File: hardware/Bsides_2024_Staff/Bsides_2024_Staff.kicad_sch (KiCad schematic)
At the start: 32 parts, among them J1 UART, J2 Battery, J3 OLED, J4 I2C, P1 USB_C_Plug_USB2.0, Q1 DMG3415U-7, SW1 ON, SW2 RESET, SW3 GPIO, SW4 RESET, SW5 RESET, SW6 RESET, SW7 RESET, U1 ESP32-C6-WROOM-1U-N4, U2 AP2112K-3.3

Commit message: feat(Hw):Init_Floorplan
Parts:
- SW1: footprint Footprint:JS102011SAQN -> bsides:MSK12C02
- SW3: value GPIO -> BOOT
- SW5, SW7: value RESET -> ~
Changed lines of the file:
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@@
 			)
 		)
-		(property "Footprint" "Footprint:JS102011SAQN"
+		(property "Footprint" "bsides:MSK12C02"
 			(at 45.339 176.276 0)
 			(effects
@@
 			)
 		)
-		(property "Value" "RESET"
+		(property "Value" "~"
 			(at 257.429 62.8904 0)
 			(effects
@@
 					(size 1.27 1.27)
 				)
+				(hide yes)
 			)
 		)
@@
 					(size 1.27 1.27)
 				)
+				(hide yes)
 			)
 		)
@@
 			)
 		)
-		(property "Value" "GPIO"
+		(property "Value" "BOOT"
 			(at 176.911 46.99 0)
 			(effects
@@
 		(dnp no)
 		(property "Reference" "SW7"
-			(at 259.461 43.815 0)
+			(at 259.334 46.228 0)
 			(effects
 				(font
@@
 			)
 		)
-		(property "Value" "RESET"
+		(property "Value" "~"
 			(at 259.461 46.1264 0)
 			(effects
@@
 					(size 1.27 1.27)
 				)
+				(hide yes)
 			)
 		)

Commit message: feat(Hw):Add_Preview
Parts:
- removed D2: RED, LED_SMD:LED_0805_2012Metric, symbol Device:LED_Small
- removed J1: UART, Connector_PinHeader_2.54mm:PinHeader_1x05_P2.54mm_Vertical, symbol Connector:Screw_Terminal_01x05
- removed J4: I2C, Connector_PinHeader_2.54mm:PinHeader_1x04_P2.54mm_Vertical, symbol Connector:Screw_Terminal_01x04
- removed R6: 330R, Resistor_SMD:R_0805_2012Metric_Pad1.20x1.40mm_HandSolder, symbol Device:R_Small
- added C10, C11, C12, C9: 0.1uF, Capacitor_SMD:C_0603_1608Metric, symbol Device:C
- added D2, D3, D4, D5: WS2812B, LED_SMD:LED_WS2812B-Mini_PLCC4_3.5x3.5mm, symbol LED:WS2812B
- added J1: Battery, bsides:BH-AAA-A1aj001, symbol Connector:Screw_Terminal_01x02
- added J4: Conn_02x03_Odd_Even, Connector_PinSocket_2.54mm:PinSocket_2x03_P2.54mm_Vertical, symbol Connector_Generic:Conn_02x03_Odd_Even
- added R7: 470, Resistor_SMD:R_0603_1608Metric, symbol Device:R
- C3, C4: value .1uF -> 0.1uF
- C5, C6, C7, C8: footprint (none) -> Capacitor_SMD:C_0603_1608Metric
- J2: footprint Footprint:BAT-TH_BH-AAA-A1AJ024 -> bsides:BH-AAA-A1aj001
- J3: footprint Connector_PinHeader_2.54mm:PinHeader_1x04_P2.54mm_Vertical -> bsides:Display OLED 128 x32
- P1: footprint Footprint:C393939 -> bsides:C393939
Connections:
- net +3V3: now also C10.2, C11.2, C12.2, C9.2, D2.1 (VDD), D3.1 (VDD), D4.1 (VDD), D5.1 (VDD)
- net GND: now also C10.1, C11.1, C12.1, C9.1, D2.3 (VSS), D3.3 (VSS), D4.3 (VSS), D5.3 (VSS), J1.1 (Pin_1); no longer J2.1 (Pin_1)
- net LED1 renamed PIN
- net PIN: now also R7.1
- new net: D2.4 (DIN), D5.2 (DOUT)
- new net: D4.2 (DOUT), D5.4 (DIN)
- new net: D3.2 (DOUT), D4.4 (DIN)
- new net: J1.2 (Pin_2), J2.1 (Pin_1)
- new net: D3.4 (DIN), R7.2
- no-connect marks 12 -> 13

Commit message: feat:(Hw)Update_PCB_Speaker_Sponsor_Staff
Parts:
- added C13: 1uF, Capacitor_SMD:C_0603_1608Metric, symbol Device:C_Small
- added C14, C15: 10uF, Capacitor_SMD:C_0603_1608Metric, symbol Device:C_Small
- J1, J2: footprint bsides:BH-AAA-A1aj001 -> bsides:BH-AA-A1AJ020; LCSC# C5290193 -> (none)
- J4: value Conn_02x03_Odd_Even -> Add_On
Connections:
- net GND: now also J4.2 (Pin_2), C13.2, C14.2, C15.2
- net SCL: now also J4.4 (Pin_4)
- net SDA: now also J4.3 (Pin_3)
- net VBUS: now also C1.1, U2.1 (VIN), U2.3 (EN); no longer D1.2 (A), Q1.1 (G), R2.1
- net VOUT: now reaches J4.1 (Pin_1)
- net VOUT: now also C10.2, C11.2, C12.2, C9.2, D2.1 (VDD), D3.1 (VDD), D4.1 (VDD), D5.1 (VDD), J3.1 (Pin_1), R1.2, R5.2, SW1.2 (B), U1.2 (3V3), C13.1, C14.1, C15.1
- removed net +3V3: C10.2, C11.2, C12.2, C2.1, C9.2, D2.1 (VDD), D3.1 (VDD), D4.1 (VDD), D5.1 (VDD), J3.1 (Pin_1), R1.2, R5.2, U1.2 (3V3), U2.5 (VOUT)
- new net: C2.1, D1.2 (A), Q1.1 (G), R2.1, U2.5 (VOUT)
- no-connect marks 13 -> 15
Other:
- moved on the sheet: D1, J1, J2, Q1, R1, R2, SW1, U1

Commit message: feat(Hw): Update schematics
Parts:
- J3: manf# I2C SH1106 Display Oled Azul 128×64 1.3 ” -> Display OLED 128×32 0.91 I2C SSD1306 Blanco / Azul
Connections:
- net GND: now also J3.4 (Pin_4); no longer J3.2 (Pin_2)
- net SCL: now also J3.2 (Pin_2); no longer J3.3 (Pin_3)
- net SDA: now also J3.1 (Pin_1); no longer J3.4 (Pin_4)
- net VOUT: now also J3.3 (Pin_3); no longer J3.1 (Pin_1)
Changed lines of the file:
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@@
 	(wire
 		(pts
+			(xy 82.55 124.46) (xy 80.01 124.46)
+		)
+		(stroke
+			(width 0)
+			(type default)
+		)
+	)
+	(wire
+		(pts
 			(xy 69.088 51.816) (xy 81.026 51.816)
 		)
@@
 	(wire
 		(pts
+			(xy 82.55 119.38) (xy 80.01 119.38)
+		)
+		(stroke
+			(width 0)
+			(type default)
+		)
+	)
+	(wire
+		(pts
 			(xy 121.412 41.91) (xy 124.46 41.91)
 		)
@@
 	(wire
 		(pts
+			(xy 82.55 116.84) (xy 80.01 116.84)
+		)
+		(stroke
+			(width 0)
+			(type default)
+		)
+	)
+	(wire
+		(pts
 			(xy 81.026 40.132) (xy 81.026 43.18)
 		)
@@
 	(wire
 		(pts
-			(xy 95.504 135.636) (xy 101.854 135.636)
-		)
-		(stroke
-			(width 0)
-			(type default)
-		)
-	)
-	(wire
-		(pts
 			(xy 54.102 178.308) (xy 54.102 176.276)
 		)
@@
 	(wire
 		(pts
-			(xy 95.504 130.556) (xy 101.854 130.556)
-		)
-		(stroke
-			(width 0)
-			(type default)
-		)
-	)
-	(wire
-		(pts
 			(xy 166.497 52.324) (xy 162.941 52.324)
 		)
@@
 	(wire
 		(pts
-			(xy 95.504 133.096) (xy 101.854 133.096)
-		)
-		(stroke
-			(width 0)
-			(type default)
-		)
-	)
-	(wire
-		(pts
 			(xy 213.614 121.539) (xy 217.424 121.539)
 		)
@@
 	(wire
 		(pts
-			(xy 95.504 128.016) (xy 101.854 128.016)
-		)
-		(stroke
-			(width 0)
-			(type default)
-		)
-	)
-	(wire
-		(pts
 			(xy 36.576 30.988) (xy 36.576 33.528)
 		)
@@
 	(wire
 		(pts
+			(xy 82.55 121.92) (xy 80.01 121.92)
+		)
+		(stroke
+			(width 0)
+			(type default)
+		)
+	)
+	(wire
+		(pts
 			(xy 262.255 87.376) (xy 265.049 87.376)
 		)
@@
 	)
 	(label "VOUT"
+		(at 80.01 121.92 180)
+		(fields_autoplaced yes)
+		(effects
+			(font
+				(size 1.27 1.27)
+			)
+			(justify right bottom)
+		)
+	)
+	(label "VOUT"
 		(at 238.252 119.888 0)
 		(fields_autoplaced yes)
@@
 		)
 	)
+	(label "SCL"
+		(at 80.01 119.38 180)
+		(fields_autoplaced yes)
+		(effects
+			(font
+				(size 1.27 1.27)
+			)
+			(justify right bottom)
+		)
+	)
 	(label "BOOT"
 		(at 35.052 70.612 0)
@@
 		)
 	)
+	(label "GND"
+		(at 80.01 124.46 180)
+		(fields_autoplaced yes)
+		(effects
+			(font
+				(size 1.27 1.27)
+			)
+			(justify right bottom)
+		)
+	)
 	(label "VOUT"
 		(at 113.792 182.626 0)
@@
 	)
 	(label "VOUT"
-		(at 95.504 128.016 0)
-		(fields_autoplaced yes)
-		(effects
-			(font
-				(size 1.27 1.27)
-			)
-			(justify left bottom)
-		)
-	)
-	(label "VOUT"
 		(at 18.034 80.264 0)
 		(fields_autoplaced yes)
@@
 		)
 	)
-	(label "GND"
-		(at 95.504 130.556 0)
-		(fields_autoplaced yes)
-		(effects
-			(font
-				(size 1.27 1.27)
-			)
-			(justify left bottom)
-		)
-	)
 	(label "EN"
 		(at 160.0454 36.576 180)
@@
 		)
 	)
-	(label "SCL"
-		(at 95.504 133.096 0)
-		(fields_autoplaced yes)
-		(effects
-			(font
-				(size 1.27 1.27)
-			)
-			(justify left bottom)
-		)
-	)
 	(label "VOUT"
 		(at 213.614 119.888 0)
@@
 		)
 	)
-	(label "RX"
-		(at 72.898 67.818 0)
+	(label "SDA"
+		(at 80.01 116.84 180)
 		(fields_autoplaced yes)
 		(effects
@@
 				(size 1.27 1.27)
 			)
-			(justify left bottom)
+			(justify right bottom)
 		)
 	)
-	(label "VOUT"
-		(at 27.432 54.61 0)
+	(label "RX"
+		(at 72.898 67.818 0)
 		(fields_autoplaced yes)
 		(effects
@@
 		)
 	)
-	(label "SDA"
-		(at 95.504 135.636 0)
+	(label "VOUT"
+		(at 27.432 54.61 0)
 		(fields_autoplaced yes)
 		(effects
@@
 	)
 	(symbol
-		(lib_id "Connector:Screw_Terminal_01x04")
-		(at 106.934 130.556 0)
-		(unit 1)
-		(exclude_from_sim no)
-		(in_bom yes)
-		(on_board yes)
-		(dnp no)
-		(fields_autoplaced yes)
-		(property "Reference" "J3"
-			(at 109.22 130.5559 0)
-			(effects
-				(font
-					(size 1.27 1.27)
-				)
-				(justify left)
-			)
-		)
-		(property "Value" "OLED"
-			(at 109.22 133.0959 0)
-			(effects
-				(font
-					(size 1.27 1.27)
-				)
-				(justify left)
-			)
-		)
-		(property "Footprint" "bsides:Display OLED 128 x32"
-			(at 106.934 130.556 0)
-			(effects
-				(font
-					(size 1.27 1.27)
-				)
-				(hide yes)
-			)
-		)
-		(property "Datasheet" "~"
-			(at 106.934 130.556 0)
-			(effects
-				(font
-					(size 1.27 1.27)
-				)
-				(hide yes)
-			)
-		)
-		(property "Description" ""
-			(at 106.934 130.556 0)
-			(effects
-				(font
-					(size 1.27 1.27)
-				)
-				(hide yes)
-			)
-		)
-		(property "manf#" "I2C SH1106 Display Oled Azul 128×64 1.3 ” "
-			(at 106.934 130.556 0)
-			(effects
-				(font
-					(size 1.27 1.27)
-				)
-				(hide yes)
-			)
-		)
-		(property "provedor" "UNIT Electronics"
-			(at 106.934 130.556 0)
-			(effects
-				(font
-					(size 1.27 1.27)
-				)
-				(hide yes)
-			)
-		)
-		(pin "1"
-		)
-		(pin "2"
-		)
-		(pin "3"
-		)
-		(pin "4"
-		)
-		(instances
-			(project "Bsides_2024_Staff"
-				(path "/93332268-4ddd-4d27-8a11-37637517d752"
-					(reference "J3")
-					(unit 1)
-				)
-			)
-		)
-	)
-	(symbol
 		(lib_id "HunterCat-NFC-rescue:USB_C_Plug_USB2.0-Connector")
 		(at 106.172 57.15 0)
@@
 					(unit 1)
 				)
+			)
+		)
+	)
+	(symbol
+		(lib_id "Connector:Screw_Terminal_01x04")
+		(at 87.63 119.38 0)
+		(unit 1)
+		(exclude_from_sim no)
+		(in_bom yes)
+		(on_board yes)
+		(dnp no)
+		(fields_autoplaced yes)
+		(property "Reference" "J3"
+			(at 89.916 119.3799 0)
+			(effects
+				(font
+					(size 1.27 1.27)
+				)
+				(justify left)
+			)
+		)
+		(property "Value" "OLED"
+			(at 89.916 121.9199 0)
+			(effects
+				(font
+					(size 1.27 1.27)
+				)
+				(justify left)
+			)
+		)
+		(property "Footprint" "bsides:Display OLED 128 x32"
+			(at 87.63 119.38 0)
+			(effects
+				(font
+					(size 1.27 1.27)
+				)
+				(hide yes)
+			)
+		)
+		(property "Datasheet" ""
+			(at 87.63 119.38 0)
+			(effects
+				(font
+					(size 1.27 1.27)
+				)
+				(hide yes)
+			)
+		)
+		(property "Description" ""
+			(at 87.63 119.38 0)
+			(effects
+				(font
+					(size 1.27 1.27)
+				)
+				(hide yes)
+			)
+		)
+		(property "manf#" "Display OLED 128×32 0.91 I2C SSD1306 Blanco / Azul"
+			(at 87.63 119.38 0)
+			(effects
+				(font
+					(size 1.27 1.27)
+				)
+				(hide yes)
+			)
+		)
+		(property "provedor" "UNIT Electronics"
+			(at 87.63 119.38 0)
+			(effects
+				(font
+					(size 1.27 1.27)
+				)
+				(hide yes)
+			)
+		)
+		(pin "1"
+		)
+		(pin "2"
+		)
+		(pin "3"
+		)
+		(pin "4"
+		)
+		(instances
+			(project "Bsides_2024_Staff"
+				(path "/93332268-4ddd-4d27-8a11-37637517d752"
+					(reference "J3")
+					(unit 1)
+				)

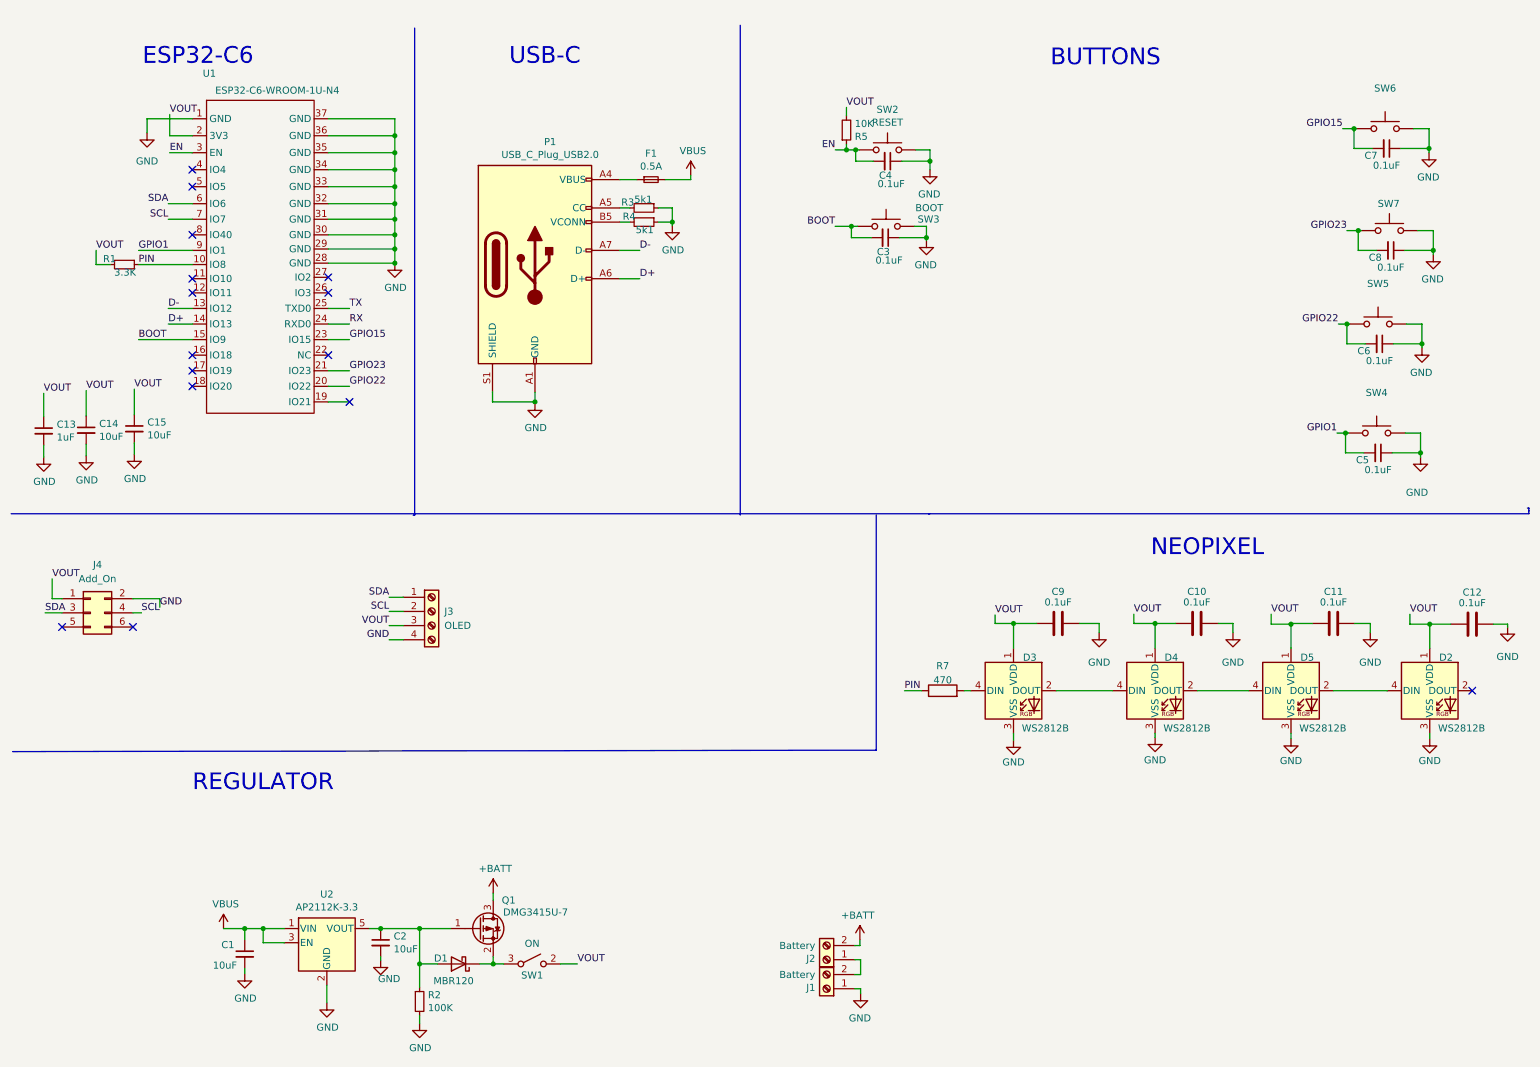
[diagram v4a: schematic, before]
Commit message: feat(Hw):Update_Staff_Sch_And_PCB
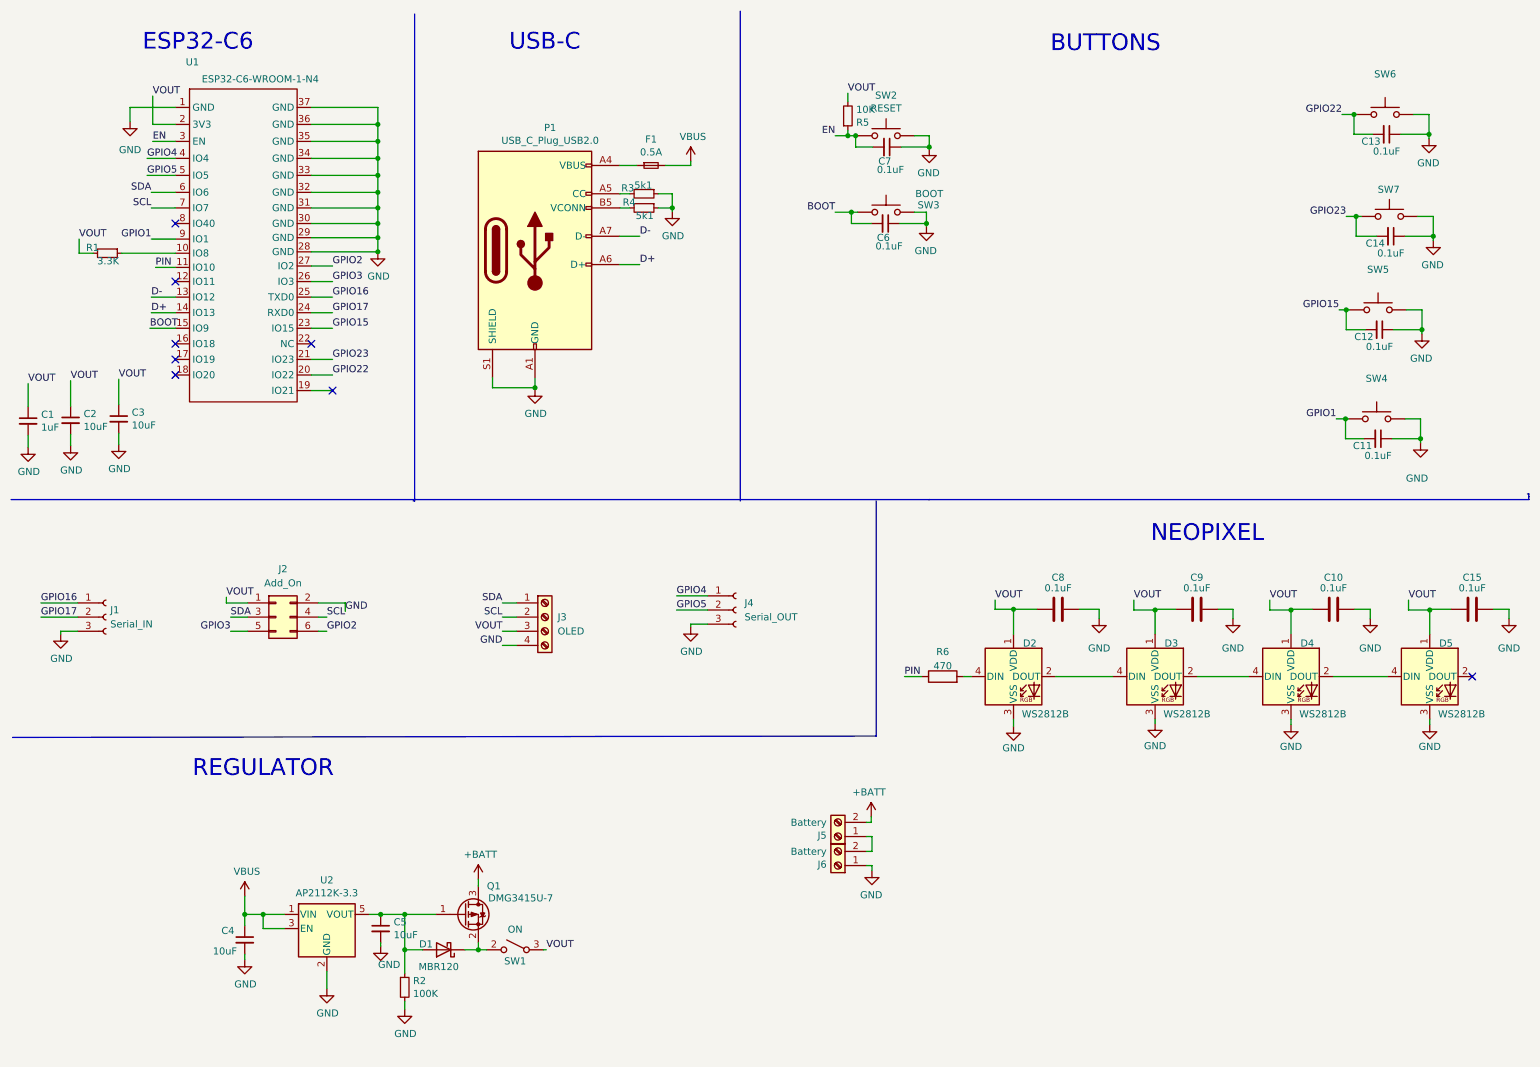
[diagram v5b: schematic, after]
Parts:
- removed C11, C12: 0.1uF, Capacitor_SMD:C_0603_1608Metric, symbol Device:C
- removed C15: 10uF, Capacitor_SMD:C_0603_1608Metric, symbol Device:C_Small
- removed C8: 0.1uF, Capacitor_SMD:C_0603_1608Metric, symbol Device:C_Small
- removed J1, J2: Battery, bsides:BH-AA-A1AJ020, symbol Connector:Screw_Terminal_01x02
- removed J4: Add_On, Connector_PinSocket_2.54mm:PinSocket_2x03_P2.54mm_Vertical, symbol Connector_Generic:Conn_02x03_Odd_Even
- removed R7: 470, Resistor_SMD:R_0603_1608Metric, symbol Device:R
- added C11, C12: 0.1uF, Capacitor_SMD:C_0603_1608Metric, symbol Device:C_Small
- added C15, C8: 0.1uF, Capacitor_SMD:C_0603_1608Metric, symbol Device:C
- added J1: Serial_IN, Connector_PinHeader_2.54mm:PinHeader_1x03_P2.54mm_Vertical, symbol Connector:Conn_01x03_Socket
- added J2: Add_On, Connector_PinSocket_2.54mm:PinSocket_2x03_P2.54mm_Vertical, symbol Connector_Generic:Conn_02x03_Odd_Even
- added J4: Serial_OUT, Connector_PinSocket_2.54mm:PinSocket_1x03_P2.54mm_Vertical, symbol Connector:Conn_01x03_Socket
- added J5, J6: Battery, bsides:BH-AA-A1AJ020, symbol Connector:Screw_Terminal_01x02
- added R6: 470, Resistor_SMD:R_0603_1608Metric, symbol Device:R
- C1: value 10uF -> 1uF; LCSC# C85713 -> C15849; Proveedor (none) -> Mouser; manf# (none) -> TMK107BJ105KA8T
- C10, C9: LCSC# C42998 -> C478888; Proveedor LCSC -> Mouser; manf# 0603F104M500NT -> KAM15AR71C104KM
- C13: value 1uF -> 0.1uF; LCSC# C15849 -> C478888; Proveedor (none) -> Mouser; manf# (none) -> KAM15AR71C104KM; provedor LCSC -> (none)
- C14: value 10uF -> 0.1uF; LCSC# C85713 -> C478888; Proveedor (none) -> Mouser; manf# (none) -> KAM15AR71C104KM; provedor LCSC -> (none)
- C2: Proveedor (none) -> Mouser; manf# (none) -> GRM188R61E106KA73J
- C3, C4: value 0.1uF -> 10uF; LCSC# C478888 -> C85713; Proveedor (none) -> Mouser; manf# (none) -> GRM188R61E106KA73J
- C5: value 0.1uF -> 10uF; LCSC# (none) -> C85713; Proveedor (none) -> Mouser; manf# (none) -> GRM188R61E106KA73J; provedor (none) -> LCSC
- C6, C7: LCSC# (none) -> C478888; Proveedor (none) -> Mouser; manf# (none) -> KAM15AR71C104KM; provedor (none) -> LCSC
- D1: Proveedor (none) -> Mouser; manf# MBR120LSF -> MBR120LSFT1G
- D2, D3, D4, D5: manf# WS2812B-Mini -> (none)
- F1: LCSC# - -> (none); Proveedor (none) -> Mouser; manf# MFU0805FF00500P100 -> MFU0805FF00750P100
- P1: Proveedor (none) -> Mouser; manf# TYPE-C-31-M-31 -> USB4105-GF-A
- Q1: Proveedor (none) -> Mouser; manf# DMG3415U-7 -> DMG3415UQ-7
- R1: Proveedor (none) -> Mouser; manf# (none) -> ERJ-3GEYJ332V
- R2: Proveedor LCSC -> Mouser; manf# (none) -> RC0603DR-07100KL
- R3, R4: Proveedor (none) -> Mouser; manf# ERJ3RBD5101V -> AC0603DR-075K1L
- R5: Proveedor (none) -> Mouser; manf# CR-03JL7---10K -> RMC1/16K1002DTP
- SW1, U2: Proveedor (none) -> Mouser
- SW2, SW3, SW5, SW7: Proveedor (none) -> Mouser; manf# (none) -> TL3342F160QG
- SW4, SW6: LCSC# C2886897 -> C318889; Proveedor (none) -> Mouser; manf# (none) -> TL3342F160QG
- U1: value ESP32-C6-WROOM-1U-N4 -> ESP32-C6-WROOM-1-N4; Proveedor (none) -> Mouser; manf# ESP32-C6-WROOM-1U-N4 -> ESP32-C6-WROOM-1-N4
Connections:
- net +BATT: now also J5.2 (Pin_2)
- net BOOT: now also C6.2; no longer C3.2
- net EN: now also C7.2; no longer C4.2
- net GND: now also C13.1, C14.1, C3.2, C4.2, C5.2, C11.1, C12.1, C15.1, C8.1, J1.3 (Pin_3), J2.2 (Pin_2), J4.3 (Pin_3), J6.1 (Pin_1); no longer C13.2, C14.2, C3.1, C4.1, C5.1
- net GPIO1: now also C11.2; no longer C5.2
- net GPIO15: now also SW5.2, C12.2; no longer C7.2, SW6.2
- net GPIO22: now also C13.2, SW6.2; no longer C6.2, SW5.2
- net GPIO23: now also C14.2
- net PIN: now also U1.11 (IO10), R6.1; no longer R1.1, U1.10 (IO8)
- net SCL: now also J2.4 (Pin_4)
- net SDA: now also J2.3 (Pin_3)
- net VBUS: now also C4.1; no longer C1.1
- net VOUT: now also C1.1, C2.1, C3.1, SW1.3 (A), C15.2, C8.2, J2.1 (Pin_1); no longer C13.1, C14.1, SW1.2 (B)
- net at D1.1 (K), Q1.2 (S): now also SW1.2 (B); no longer SW1.3 (A)
- net at D5.2 (DOUT): no longer D2.4 (DIN)
- net GPIO3: now reaches U1.26 (IO3)
- net GPIO3: now also J2.5 (Pin_5)
- net GPIO2: now reaches U1.27 (IO2)
- net GPIO2: now also J2.6 (Pin_6)
- net GPIO4: now reaches U1.4 (IO4)
- net GPIO4: now also J4.1 (Pin_1)
- net GPIO5: now reaches U1.5 (IO5)
- net GPIO5: now also J4.2 (Pin_2)
- net at D1.2 (A), Q1.1 (G), R2.1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: now also C5.1; no longer C2.1
- net at D2.2 (DOUT): now also D3.4 (DIN)
- net RX renamed GPIO17
- net GPIO17: now also J1.2 (Pin_2)
- net TX renamed GPIO16
- net GPIO16: now also J1.1 (Pin_1)
- new net: J5.1 (Pin_1), J6.2 (Pin_2)
- new net: R1.1, U1.10 (IO8)
- new net: D2.4 (DIN), R6.2
- no-connect marks 15 -> 8

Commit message: feat(Hw):First_Route_Staff
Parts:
- J1: footprint Connector_PinHeader_2.54mm:PinHeader_1x03_P2.54mm_Vertical -> Connector_PinSocket_2.54mm:PinSocket_1x03_P2.54mm_Vertical
- J4: footprint Connector_PinSocket_2.54mm:PinSocket_1x03_P2.54mm_Vertical -> Connector_PinHeader_2.54mm:PinHeader_1x03_P2.54mm_Vertical
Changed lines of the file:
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@@
 			)
 		)
-		(property "Footprint" "Connector_PinHeader_2.54mm:PinHeader_1x03_P2.54mm_Vertical"
+		(property "Footprint" "Connector_PinSocket_2.54mm:PinSocket_1x03_P2.54mm_Vertical"
 			(at 29.21 120.396 0)
 			(effects
@@
 			)
 		)
-		(property "Footprint" "Connector_PinSocket_2.54mm:PinSocket_1x03_P2.54mm_Vertical"
+		(property "Footprint" "Connector_PinHeader_2.54mm:PinHeader_1x03_P2.54mm_Vertical"
 			(at 142.24 119.126 0)
 			(effects
@@
 			)
 		)
-		(property "Datasheet" "~"
+		(property "Datasheet" ""
 			(at 142.24 119.126 0)
 			(effects
